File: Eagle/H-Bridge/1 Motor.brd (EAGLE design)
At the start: 65 x 34 mm, 10 parts, among them K1 CQ1-12V, K2 CQ1-12V, T3 TIP122

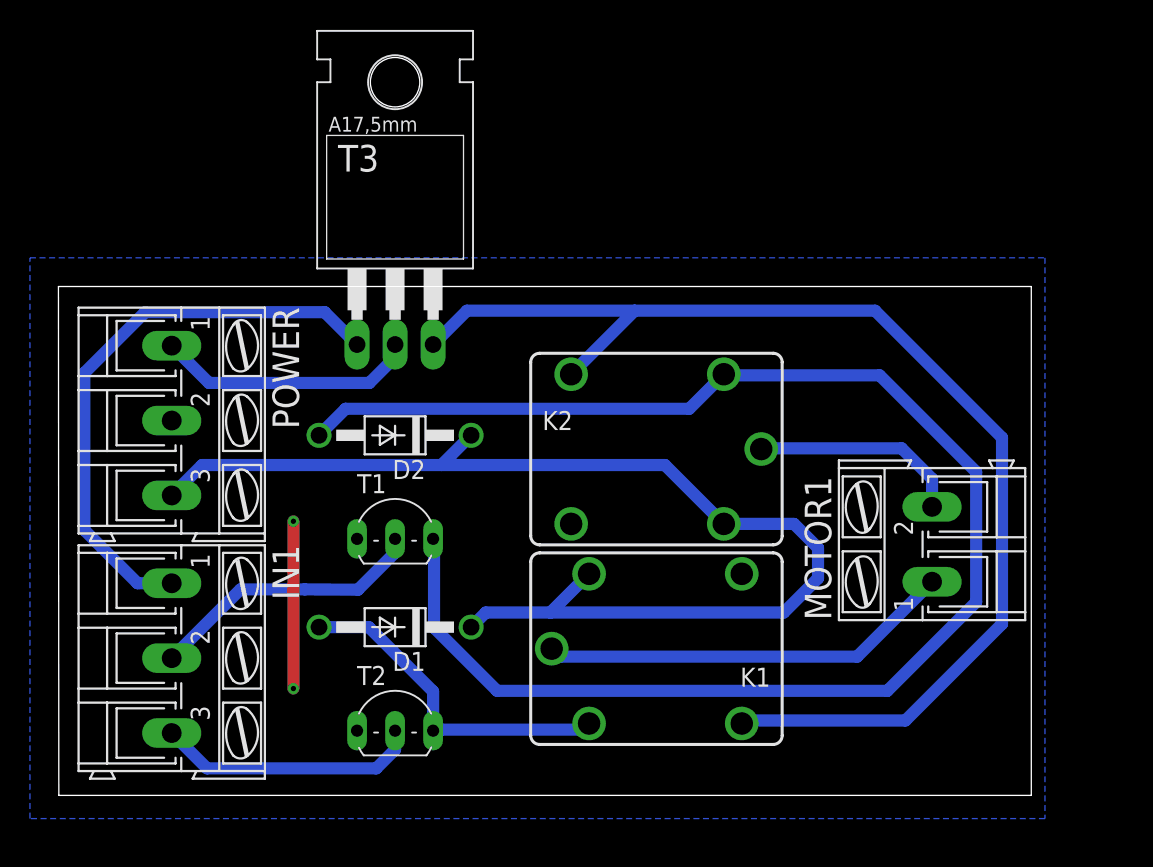
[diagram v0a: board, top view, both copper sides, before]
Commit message: re-arrange items and use the right package of the relay.
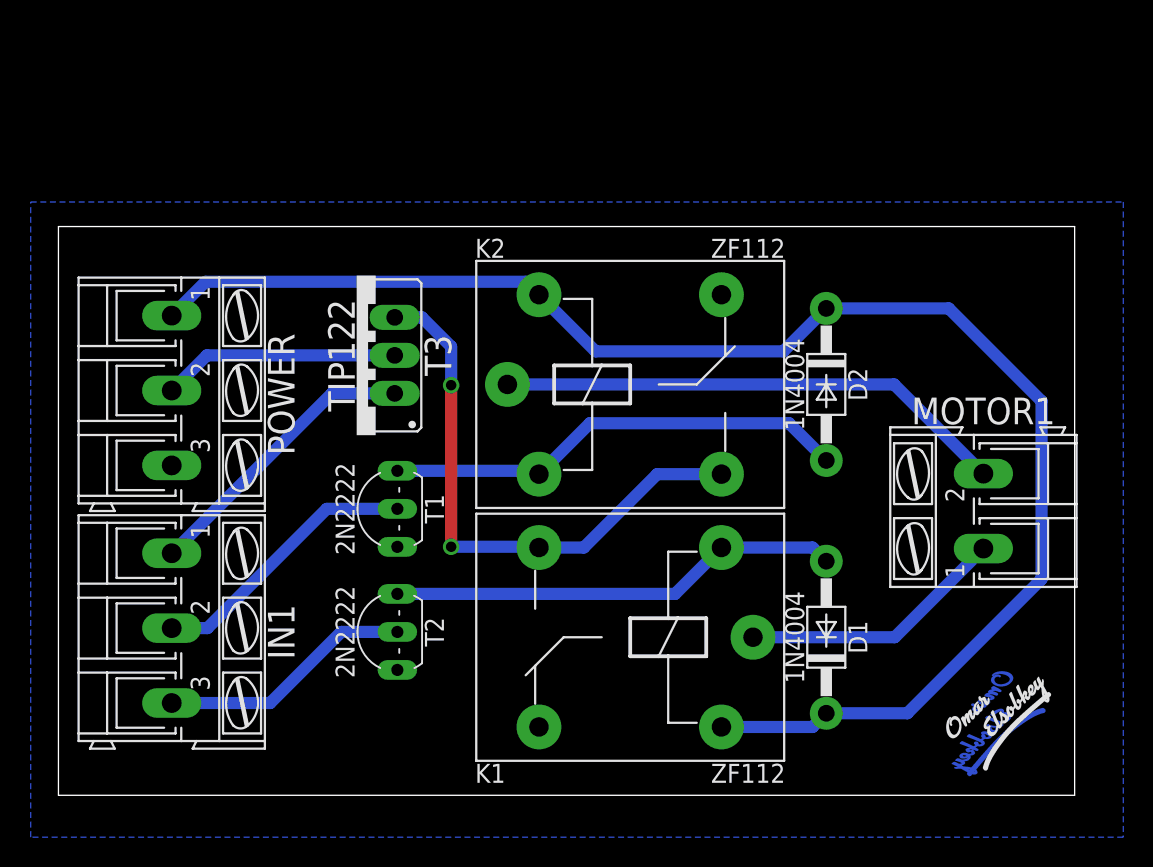
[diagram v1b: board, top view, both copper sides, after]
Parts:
- added U$1: (no value), Logos:OMAR_ELSOBKEY_X0.5_T
- added U$2: (no value), Logos:OMAR_ELSOBKEY_X0.5_TN
- K1, K2: value CQ1-12V -> ZF112; device relay:CQ1 -> relay:ZF112
- T1, T2: value (none) -> 2N2222
- moved D2 29.0 mm to (51.3, 27.5), turned to 270 degrees
- moved D1 28.8 mm to (51.3, 10.6), turned to 90 degrees
- moved T3 7.07 mm to (22.5, 29.4), turned to 90 degrees
- moved T2 5.44 mm to (21.4, 10.9), turned to 90 degrees
- moved K2 4.66 mm to (38.2, 27.5)
- moved MOTOR1 4.08 mm to (61.8, 19.0)
- moved IN1 2.01 mm to (7.57, 11.2)
- moved POWER 2.01 mm to (7.57, 27.1)
- moved K1 1.91 mm to (38.2, 10.6)
- moved T1 1.34 mm to (21.4, 19.1), turned to 90 degrees
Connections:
- removed net N$3: K1.NO, K2.NO, T3.3
- new net NO: K1.S, K2.S, T3.3
- net +12V: now also POWER.2; no longer POWER.1
- net +5V: now also POWER.1; no longer POWER.3
- net GND: now also K1.O, K2.O, POWER.3; no longer K1.NC, K2.NC, POWER.2
- net N$1: now also K2.P; no longer K2.C
- net N$5: now also K1.P; no longer K1.C
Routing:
- net N$3: track 81.1 -> 0.00 mm
- net N$6: track 103.4 -> 31.2 mm
- net NO: track 0.00 -> 38.1 mm, vias 0 -> 2
- net +5V: track 79.5 -> 102.1 mm
- net N$1: track 14.2 -> 34.3 mm
- net EN: track 38.6 -> 19.3 mm
- net GND: track 11.2 -> 0.00 mm, vias 2 -> 0
- net N$5: track 27.7 -> 17.8 mm
- net N$4: track 22.6 -> 30.3 mm
- net +12V: track 17.5 -> 15.9 mm
- net IN2: track 17.7 -> 17.0 mm
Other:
- board size 65 x 34 mm -> 67.9 x 38 mm
